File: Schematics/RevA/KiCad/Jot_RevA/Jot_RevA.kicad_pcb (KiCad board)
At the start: 4 copper layers, 37 x 62.6 mm, 83 parts, among them J1 USB-C, J2 Battery, Q1 AO3400A, Q2 AO3401A, Q3 AO3400A, Q4 AO3400A, Q5 AO3400A, Q6 AO3401A, Q7 AO3400A, Q8 AO3400A, SW1 SW_Push, U1 MDBT50Q-1MV2, U10 USBLC6-2SC6, U2 MMICT3902-00-012, U3 MMICT3902-00-012, U4 W25Q256JVEIQ, U5 MCP73831T-2ACI/OT, U6 MAX17048, U7 LIS2DW12TR, U8 DRV2605LDGS, U9 TPS7A0233, Y1 32.768kHz

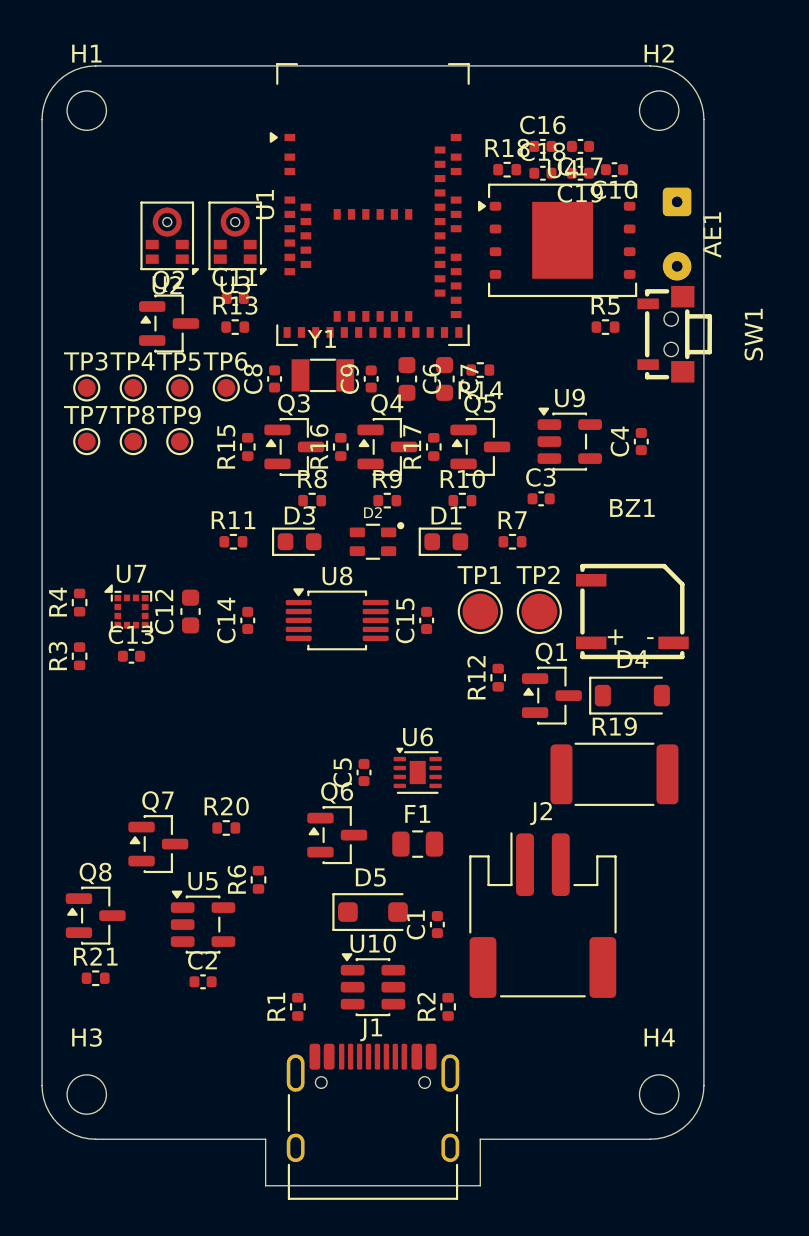
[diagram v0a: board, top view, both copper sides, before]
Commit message: Rev A layout: net classes, ground plane and vias, main 5 V path; NFC paperwork
- Net classes: Default 0.2 mm / 0.15 mm clearance; Power 0.5 mm for VBUS,
  +BATT, BATT_RAW, BATT_FUSED and the buzzer nets
- In1.Cu solid GND zone (antenna keep-out respected); U7 pad clearance
  override removed
- 43 GND vias, every GND pad tied to the plane on F.Cu, no via-in-pad
- VBUS: J1 -> D5 -> C1 and across to the charger U5, 0.5 mm on F.Cu, kept
  clear of the USB CC and data pins; J1's second VBUS pin and U10 pin 5 to
  follow on B.Cu
- BOM and JLCPCB BOM: C16/C17 82 pF YAGEO CC0402JRNPO9BN820 (C107011),
  C18/C19 DNP tuning pads, AE1 Molex 146236-0101 bought separately
- Architecture draft 6: NFC section rewritten for the flex antenna
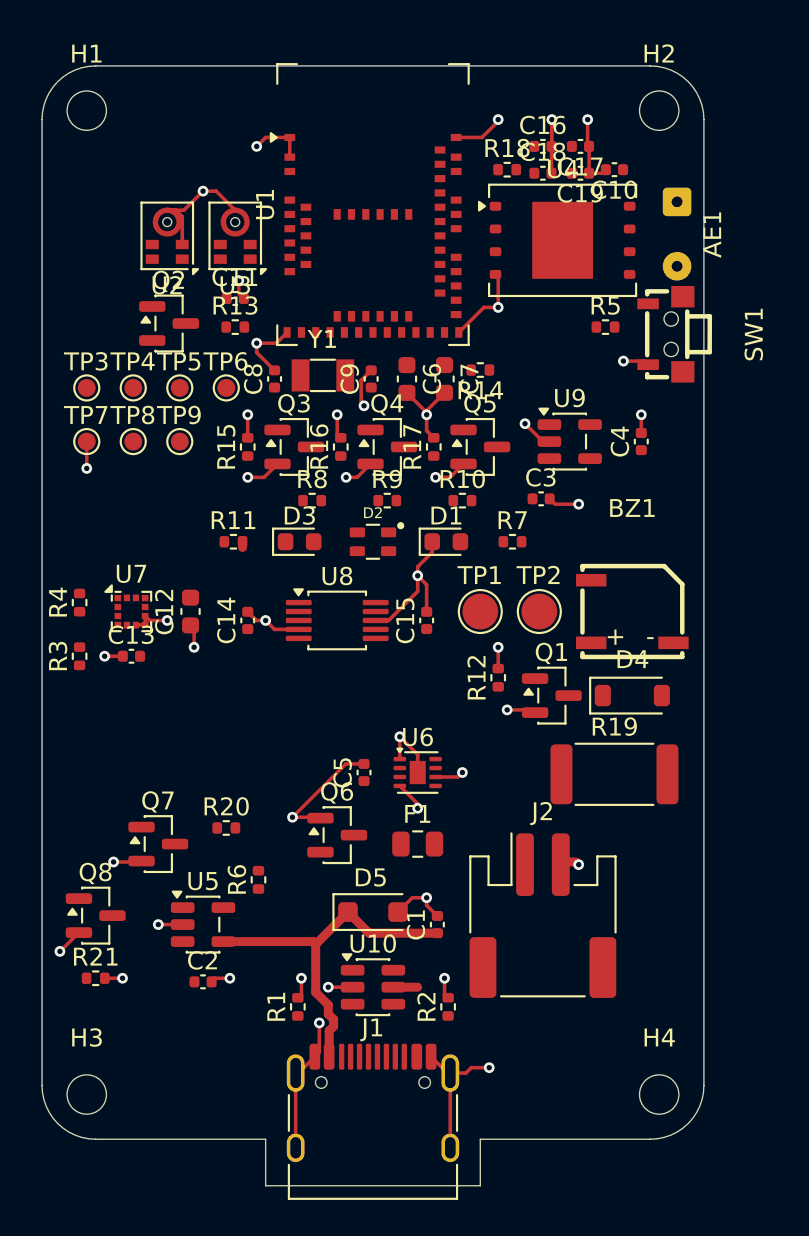
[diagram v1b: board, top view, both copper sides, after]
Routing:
- net GND: track 0.00 -> 115.6 mm, vias 0 -> 43
- net VBUS: track 0.00 -> 21.8 mm
- added copper zone on In1.Cu, net GND

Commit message: Rev A layout: USB-C corner routed
- D- pins B7/A7 joined on B.Cu through vias under the receptacle; D+ pins
  A6/B6 bridged on F.Cu into U10 pin 3; D- into U10 pin 1
- CC1 to R1 (moved beside U10); CC2 to R2 on B.Cu below the pin row
- U10 pin 5 VBUS threaded between the USB_DM/USB_DP escape vias and down to
  J1's second VBUS pin
- USB_DM/USB_DP escape vias right of U10 for the run to the module
- Leftover GND and VBUS stubs removed
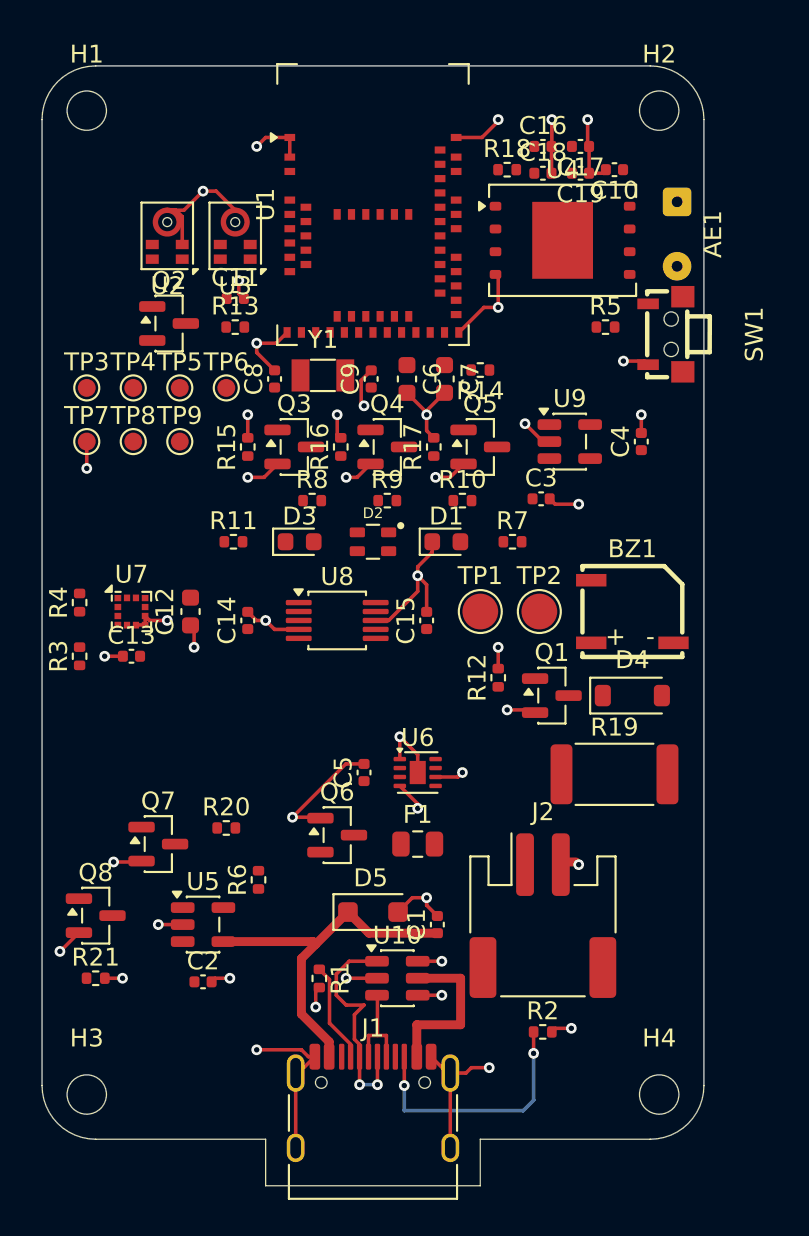
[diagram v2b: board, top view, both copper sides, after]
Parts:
- moved R2 5.47 mm to (109.5, 124.0), turned to 0 degrees
- moved R1 1.99 mm to (97.0, 121.0), turned to -90 degrees
- moved U10 1.45 mm to (101.4, 121.0)
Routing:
- net Net-(J1-CC2): track 0.00 -> 14.3 mm, vias 0 -> 2
- net Net-(J1-D--PadA7): track 0.00 -> 12.9 mm, vias 0 -> 2
- net VBUS: track 21.8 -> 29.8 mm
- net Net-(J1-D+-PadA6): track 0.00 -> 5.63 mm
- net Net-(J1-CC1): track 0.00 -> 5.61 mm
- net GND: track 115.6 -> 117.8 mm
- net USB_DP: track 0.00 -> 1.35 mm, vias 0 -> 1
- net USB_DM: track 0.00 -> 1.35 mm, vias 0 -> 1

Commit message: Rev A layout: USB data routed to the module
- USB_DM/USB_DP run as a pair on B.Cu from U10 to the module, about 0.35 mm
  apart; vias outside the module, short F.Cu entries into pins 34 and 35
- Module pin 33 and U4 pin 4 given their own GND vias to clear the path
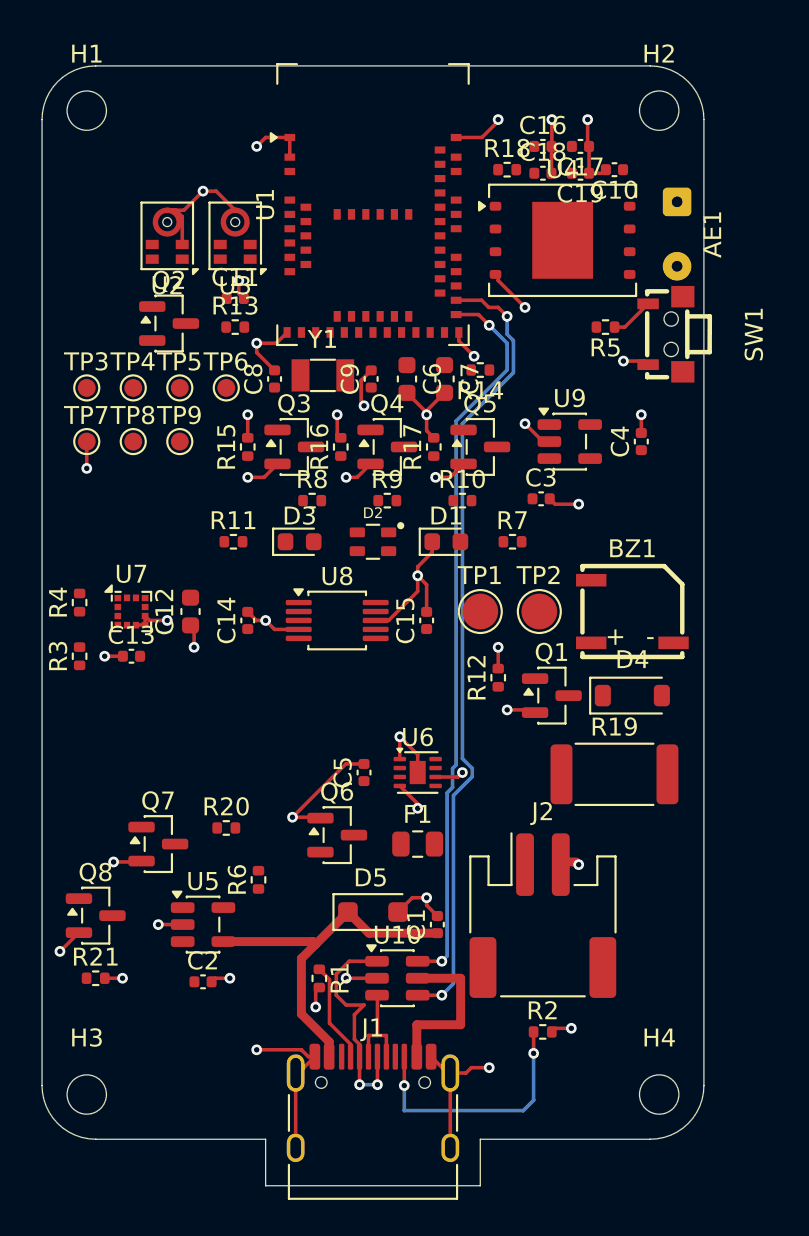
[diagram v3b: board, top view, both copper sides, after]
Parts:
- turned R5 to 180 degrees
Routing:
- net USB_DP: track 1.35 -> 45.0 mm, vias 1 -> 2
- net USB_DM: track 1.35 -> 40.9 mm, vias 1 -> 2
- net Net-(R5-Pad1): track 0.00 -> 2.51 mm
- net GND: track 117.8 -> 117.3 mm, vias 43 -> 44

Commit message: Rev A layout: power planes, power vias and first layout review fixes
- In2.Cu: +3V3 zone (top + left strip, with a +BATT corridor under the USB
  pair) over a board-wide +BATT zone; every +3V3/+BATT pad via-tied
- Plane clearance 0.25 mm; extra all-layer antenna clearance areas beside
  the module along the top edge (Raytac 2.3)
- C1 moved beside U5 VDD; D5 moved next to J1 VBUS; second +BATT via at Q6;
  U5 GND widened; J1's two VBUS pins joined on B.Cu
- U8 pin 10 tied to +BATT with a 0.25 mm stub
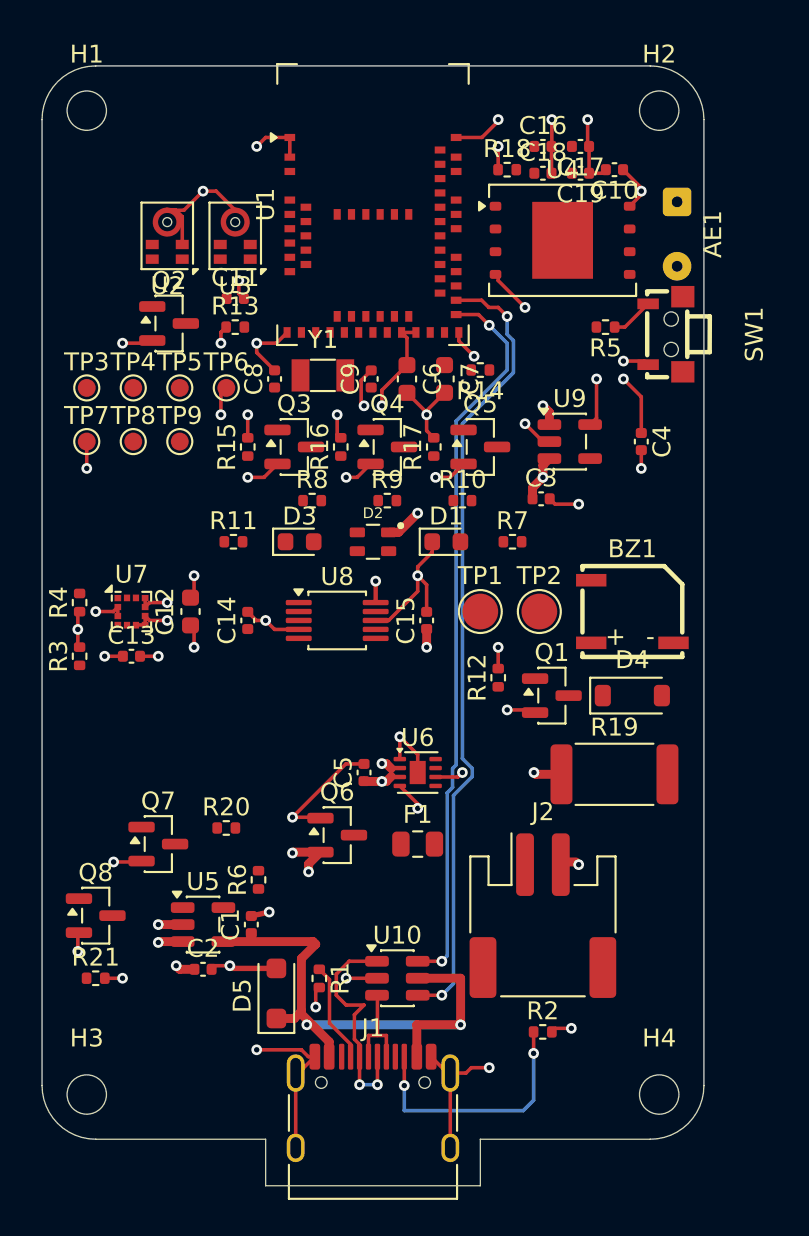
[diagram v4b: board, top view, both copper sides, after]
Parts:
- moved C1 10.4 mm to (93.2, 118.0)
- moved D5 7.06 mm to (94.6, 121.8), turned to 90 degrees
- moved C2 0.70 mm to (90.5, 120.5)
- turned C4 to -90 degrees
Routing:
- net +3V3: track 0.00 -> 28.2 mm, vias 0 -> 13
- net +BATT: track 0.00 -> 17.4 mm, vias 0 -> 12
- net VBUS: track 29.8 -> 32.4 mm, vias 0 -> 2
- added copper zone on In2.Cu, net +3V3
- added copper zone on In2.Cu, net +BATT

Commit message: Rev A layout: battery path, crystal and NFC routed
- BATT_RAW J2 -> F1 and BATT_FUSED F1 -> Q6 at 0.5 mm on F.Cu
- 32.768 kHz crystal: module pins straight down to Y1, then C8/C9; C9 GND
  via moved clear of the crystal path
- NFC1 escapes inward under the module to B.Cu; NFC2 over the outer pads;
  NFC2 to AE1 runs on B.Cu under U4
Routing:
- net NFC1: track 0.00 -> 20.6 mm, vias 0 -> 2
- net NFC2: track 0.00 -> 18.0 mm, vias 0 -> 1
- net /Power/BATT_RAW: track 0.00 -> 8.88 mm
- net Net-(U1-P0.01): track 0.00 -> 6.69 mm
- net /Power/BATT_FUSED: track 0.00 -> 6.21 mm
- net Net-(U1-P0.00): track 0.00 -> 4.48 mm
- net GND: track 117.4 -> 116.8 mm

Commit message: Rev A layout: RGB LED turned 180 degrees so its cathodes line up with R8-R10
- D2 rotated in place under the middle front dot; +BATT anode via moved
  below-left; old anode stub removed
- LED gate pull-downs connected
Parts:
- turned D2 to 180 degrees
- turned R7 to 180 degrees
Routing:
- net LED_R: track 0.00 -> 2.27 mm
- net LED_G: track 0.00 -> 2.27 mm
- net +BATT: track 17.4 -> 16.6 mm
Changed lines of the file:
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@@
 	(footprint "Resistor_SMD:R_0402_1005Metric"
 		(layer "F.Cu")
-		(at 107.8 96.6)
+		(at 107.8 96.6 180)
 		(descr "Resistor SMD 0402 (1005 Metric), square (rectangular) end terminal, IPC-7351 nominal, (Body size source: IPC-SM-782 page 72, https://www.pcb-3d.com/wordpress/wp-content/uploads/ipc-sm-782a_amendment_1_and_2.pdf)")
 		(tags "resistor")
@@
 		(duplicate_pad_numbers_are_jumpers no)
 		(fp_line
-			(start -0.153641 -0.38)
-			(end 0.153641 -0.38)
+			(start -0.153641 0.38)
+			(end 0.153641 0.38)
 			(stroke
 				(width 0.12)
@@
 		)
 		(fp_line
-			(start -0.153641 0.38)
-			(end 0.153641 0.38)
+			(start -0.153641 -0.38)
+			(end 0.153641 -0.38)
 			(stroke
 				(width 0.12)
@@
 		)
 		(pad "1" smd roundrect
-			(at -0.51 0)
+			(at -0.51 0 180)
 			(size 0.54 0.64)
 			(layers "F.Cu" "F.Mask" "F.Paste")
@@
 		)
 		(pad "2" smd roundrect
-			(at 0.51 0)
+			(at 0.51 0 180)
 			(size 0.54 0.64)
 			(layers "F.Cu" "F.Mask" "F.Paste")
@@
 		(locked yes)
 		(layer "F.Cu")
-		(at 100 96.6)
+		(at 100 96.6 180)
 		(descr "TOGIALED TJ-S1615SW6TGLCC*RGB-A5, 1.6x1.5 mm 4-pad RGB LED. Pads from datasheet 'Recommend Pad Layout': 2.60 x 1.60 overall, 0.90 gap between columns, 0.50 gap between rows -> 0.85 x 0.55 mm pads. Top view: pad 1 top-right (common anode on the CY part), 2 top-left, 3 bottom-left, 4 bottom-right.")
 		(tags "LED RGB 1615 TOGIALED")
 		(property "Reference" "D2"
-			(at 0 -1.6 0)
+			(at 0 -1.6 180)
 			(layer "F.SilkS")
 			(effects
@@
 		)
 		(property "Value" "TJ-S1615SW6TGLCCYRGB-A5"
-			(at 0 1.6 0)
+			(at 0 1.6 180)
 			(layer "F.Fab")
 			(effects
@@
 		)
 		(property "Datasheet" "${KIPRJMOD}/../../Datasheets/UI/TJ-S1615SW6TGLCCYRGB-A5_RGB_LED.pdf"
-			(at 0 0 0)
+			(at 0 0 180)
 			(layer "F.Fab")
 			(hide yes)
@@
 		)
 		(property "Description" "TOGIALED RGB LED, common anode, 1.6x1.5 mm SMD-4 (pin 1 anode, 2 blue, 3 green, 4 red cathode); LCSC C273610"
-			(at 0 0 0)
+			(at 0 0 180)
 			(layer "F.Fab")
 			(hide yes)
@@
 		(duplicate_pad_numbers_are_jumpers no)
 		(fp_line
-			(start -0.35 -0.95)
-			(end 0.35 -0.95)
+			(start -0.35 0.95)
+			(end 0.35 0.95)
 			(stroke
 				(width 0.12)
@@
 		)
 		(fp_line
-			(start -0.35 0.95)
-			(end 0.35 0.95)
+			(start -0.35 -0.95)
+			(end 0.35 -0.95)
 			(stroke
 				(width 0.12)
@@
 		)
 		(fp_line
-			(start -0.8 -0.75)
-			(end 0.8 -0.75)
+			(start 0.8 0.75)
+			(end -0.8 0.75)
 			(stroke
 				(width 0.1)
@@
 		)
 		(fp_line
-			(start -0.8 0.75)
-			(end -0.8 -0.75)
+			(start 0.8 -0.75)
+			(end 0.8 0.75)
 			(stroke
 				(width 0.1)
@@
 		)
 		(fp_line
-			(start 0.8 -0.75)
-			(end 0.8 0.75)
+			(start -0.8 0.75)
+			(end -0.8 -0.75)
 			(stroke
 				(width 0.1)
@@
 		)
 		(fp_line
-			(start 0.8 0.75)
-			(end -0.8 0.75)
+			(start -0.8 -0.75)
+			(end 0.8 -0.75)
 			(stroke
 				(width 0.1)
@@
 		)
 		(pad "1" smd roundrect
-			(at 0.875 -0.525)
+			(at 0.875 -0.525 180)
 			(size 0.85 0.55)
 			(layers "F.Cu" "F.Mask" "F.Paste")
@@
 		)
 		(pad "2" smd roundrect
-			(at -0.875 -0.525)
+			(at -0.875 -0.525 180)
 			(size 0.85 0.55)
 			(layers "F.Cu" "F.Mask" "F.Paste")
@@
 		)
 		(pad "3" smd roundrect
-			(at -0.875 0.525)
+			(at -0.875 0.525 180)
 			(size 0.85 0.55)
 			(layers "F.Cu" "F.Mask" "F.Paste")
@@
 		)
 		(pad "4" smd roundrect
-			(at 0.875 0.525)
+			(at 0.875 0.525 180)
 			(size 0.85 0.55)
 			(layers "F.Cu" "F.Mask" "F.Paste")
@@
 	)
 	(segment
-		(start 99.52 110)
-		(end 99.5 109.98)
-		(width 0.5)
+		(start 99.8625 90.35)
+		(end 98.4025 91.81)
+		(width 0.2)
 		(layer "F.Cu")
-		(net "+BATT")
+		(net "LED_G")
+	)
+	(segment
+		(start 98.4025 91.81)
+		(end 98.2 91.81)
+		(width 0.2)
+		(layer "F.Cu")
+		(net "LED_G")
 	)
 	(segment
-		(start 101.425 96.075)
-		(end 102.5 95)
+		(start 99.52 110)
+		(end 99.5 109.98)
 		(width 0.5)
 		(layer "F.Cu")
@@
 	)
 	(segment
-		(start 100.875 96.075)
-		(end 101.425 96.075)
+		(start 99.12 97.12)
+		(end 98.3 98)
 		(width 0.5)
 		(layer "F.Cu")
@@
 	)
 	(via
+		(at 98.3 98)
+		(size 0.6)
+		(drill 0.3)
+		(layers "F.Cu" "B.Cu")
+		(net "+BATT")
+	)
+	(via
 		(at 96.4 115.05)
 		(size 0.6)
@@
 	)
 	(via
-		(at 102.5 95)
-		(size 0.6)
-		(drill 0.3)
-		(layers "F.Cu" "B.Cu")
-		(net "+BATT")
-	)
-	(via
 		(at 95.5 114)
 		(size 0.6)
@@
 	)
 	(segment
+		(start 94.6625 90.35)
+		(end 93.2025 91.81)
+		(width 0.2)
+		(layer "F.Cu")
+		(net "LED_R")
+	)
+	(segment
+		(start 93.2025 91.81)
+		(end 93 91.81)
+		(width 0.2)
+		(layer "F.Cu")
+		(net "LED_R")
+	)
+	(segment
